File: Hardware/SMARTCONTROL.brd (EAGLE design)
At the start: 40 x 54 mm, 36 parts, among them IC1 ESP12-SMT, J1 ESPFLASH-1X6-2.54-SOCKET, Q2 RJU003N03, Q3 RJU003N03, Q4 RJU003N03, Q5 RJU003N03

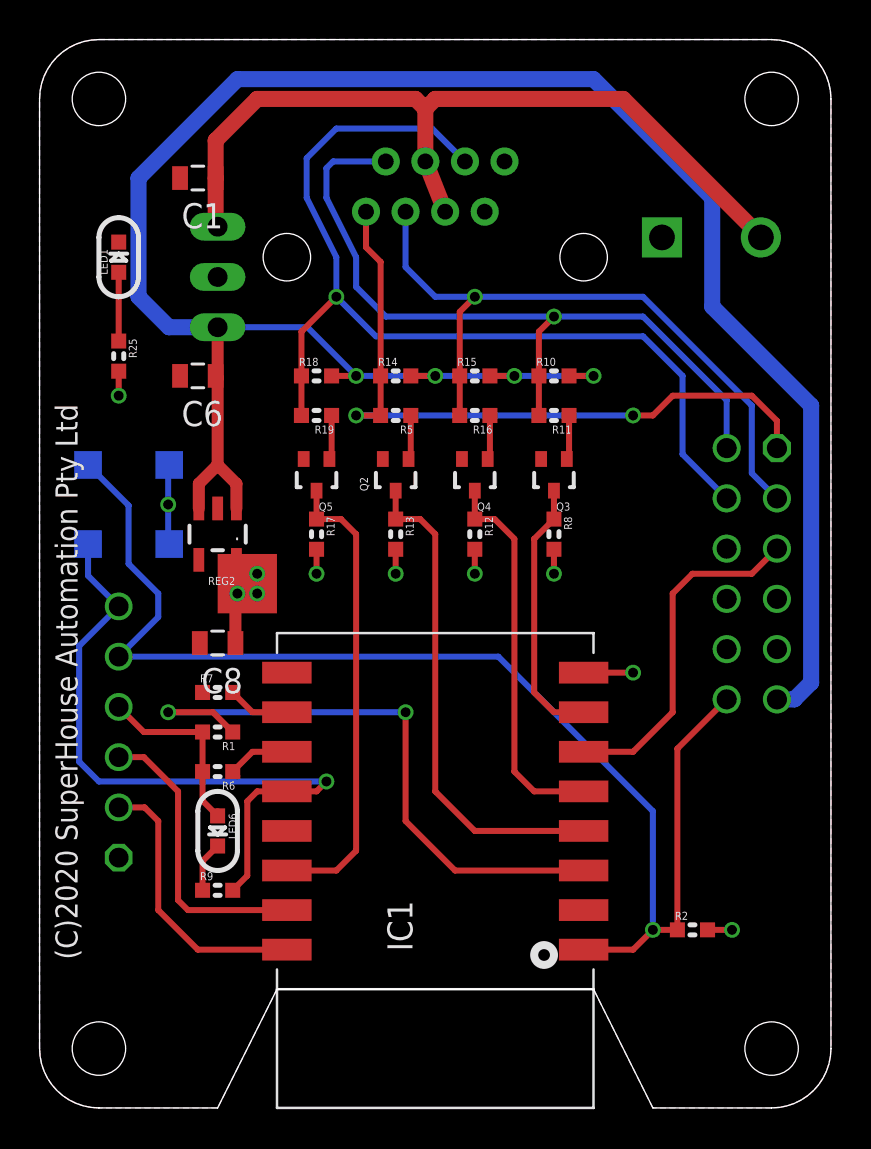
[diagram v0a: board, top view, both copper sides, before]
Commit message: Converted switch isolation from FETs to diodes for v2.1 release.
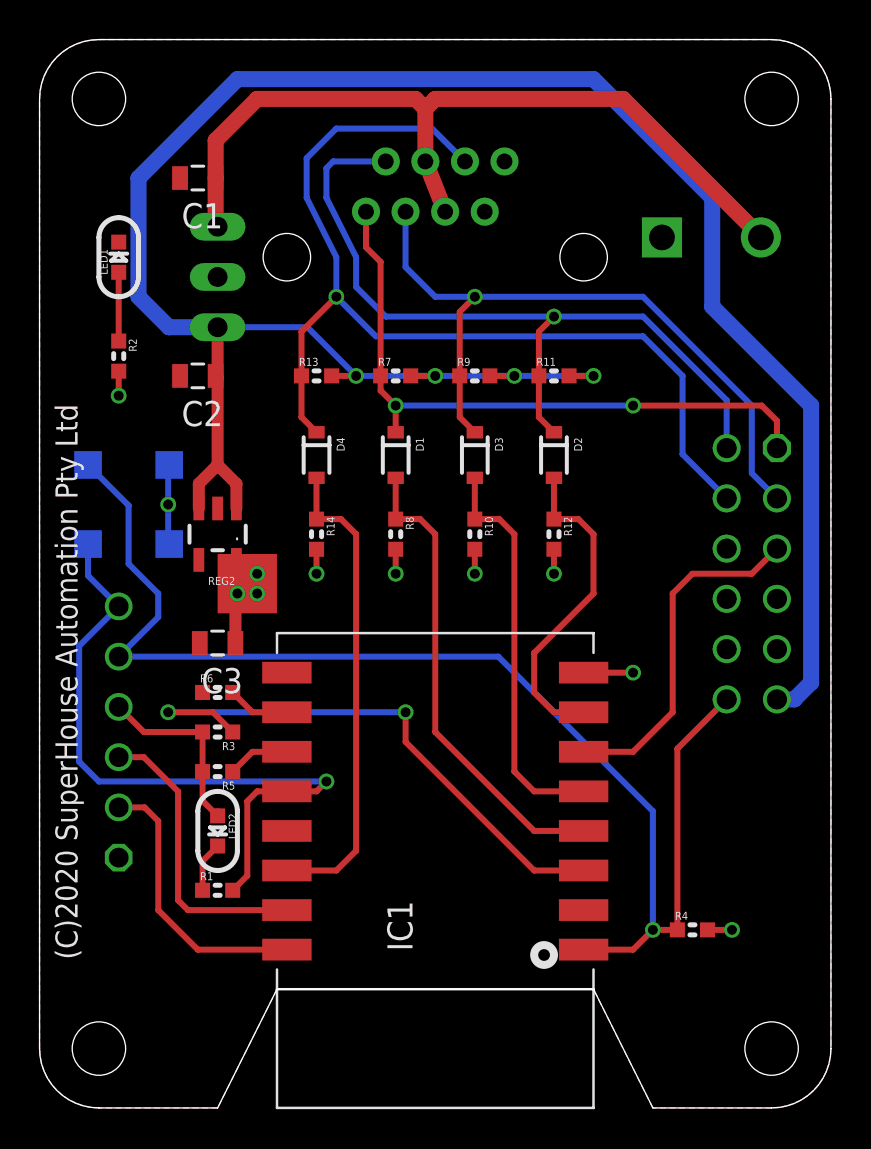
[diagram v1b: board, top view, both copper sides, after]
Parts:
- removed Q2, Q3, Q4, Q5: RJU003N03, SuperHouse-DiscreteSemi:SOT32-3
- removed R15, R17, R18: 22K, SuperHouse-DiscreteSemi:R0603
- removed R16, R19: 1K, SuperHouse-DiscreteSemi:R0603
- removed R25: 4K7, SuperHouse-DiscreteSemi:R0603
- added D1, D2, D3, D4: 1N4148WS, SuperHouse-DiscreteSemi:SOD-323
- added R3, R4: 10k, SuperHouse-DiscreteSemi:R0603
- R1: value 10k -> 1K
- R10, R12, R13, R14, R8: value 22K -> 10K
- R11, R9: value 1K -> 10K
- R2: value 10k -> 4K7
- R5: value 1K -> 10k
- R7: value 10k -> 10K
- moved R2 41.0 mm to (4.00, 38.0), turned to 270 degrees
- moved R9 29.1 mm to (22.0, 37.0)
- moved R5 20.1 mm to (9.00, 17.0)
- moved R7 18.4 mm to (18.0, 37.0)
- moved R10 8.94 mm to (22.0, 29.0), turned to 270 degrees
- moved R13 8.94 mm to (14.0, 37.0), turned to 0 degrees
- moved R14 8.94 mm to (14.0, 29.0), turned to 270 degrees
- moved R1 8.00 mm to (9.00, 11.0), turned to 0 degrees
- moved R8 8.00 mm to (18.0, 29.0)
- moved R12 4.00 mm to (26.0, 29.0)
- moved R6 4.00 mm to (9.00, 21.0), turned to 0 degrees
- moved R11 2.00 mm to (26.0, 37.0), turned to 0 degrees
- renumbered C6 to C2, C8 to C3, JP4 to J2, LED6 to LED2, S3 to J3
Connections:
- removed net N$1: Q2.1, R5.1
- removed net N$2: Q3.1, R11.1
- removed net N$3: Q4.1, R16.1
- removed net N$4: Q5.1, R19.1
- net !RESET: now also R4.1; no longer R2.1
- net 3.3V: now also R10.2, R14.2, R3.2, R4.2, R5.2; no longer R1.2, R13.2, R17.2, R25.2, R6.2
- net 5V: now also R11.2, R13.2, R7.2, R9.2; no longer R10.2, R14.2, R15.2, R18.2
- net BUTTON1: now also D1.1, R7.1; no longer R14.1, R5.2
- net BUTTON2: now also D2.1, R11.1; no longer R10.1, R11.2
- net BUTTON3: now also D3.1, R9.1; no longer R15.1, R16.2
- net BUTTON4: now also D4.1, R13.1; no longer R18.1, R19.2
- net CH_PD: now also R3.1; no longer R1.1
- net GND: now also R6.1; no longer Q2.2, Q3.2, Q4.2, Q5.2, R7.1
- net GPIO0: now also R1.2; no longer R9.2
- net GPIO13: now also D2.2, R12.1; no longer Q3.3, R8.1
- net GPIO14: now also D3.2, R10.1; no longer Q4.3, R12.1
- net GPIO15: now also R6.2; no longer R7.2
- net GPIO16: now also D1.2, R8.1; no longer Q2.3, R13.1
- net GPIO2: now also R5.1; no longer R6.1
- net GPIO5: now also D4.2, R14.1; no longer Q5.3, R17.1
- net N$23: now also R2.1; no longer R25.1
- net N$27: now also R1.1; no longer R9.1
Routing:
- net GPIO13: track 13.5 -> 16.6 mm
- net BUTTON1: track 35.4 -> 32.7 mm
- net N$4: track 2.41 -> 0.00 mm
- net CH_PD: track 31.2 -> 28.9 mm
- net N$3: track 2.25 -> 0.00 mm
- net N$2: track 2.25 -> 0.00 mm
- net N$1: track 2.25 -> 0.00 mm
- net BUTTON4: track 49.7 -> 50.8 mm
- net BUTTON3: track 34.7 -> 35.9 mm
- net BUTTON2: track 38.3 -> 39.5 mm
- net GPIO16: track 25.1 -> 24.0 mm
- net GPIO14: track 19.5 -> 20.3 mm
- net GPIO5: track 23.7 -> 24.3 mm
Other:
- board text added: "v2.1"
- board text removed: "v2.0"
